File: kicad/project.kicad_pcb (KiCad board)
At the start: 2 copper layers, 22 parts, among them J1 SWD, SW1 SW_DPDT_x2, U1 STM32L031F4Px

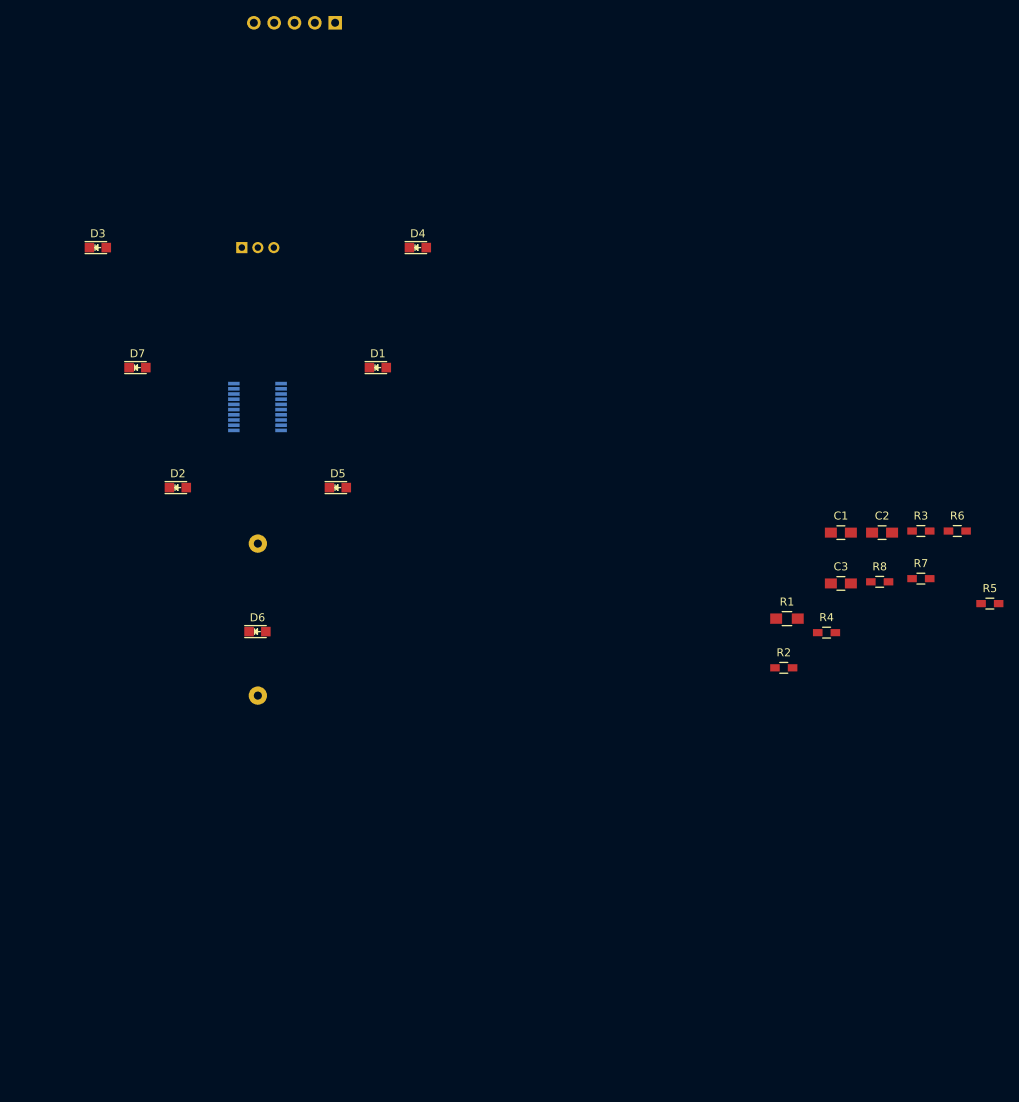
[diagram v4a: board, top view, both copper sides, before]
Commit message: Heart outline
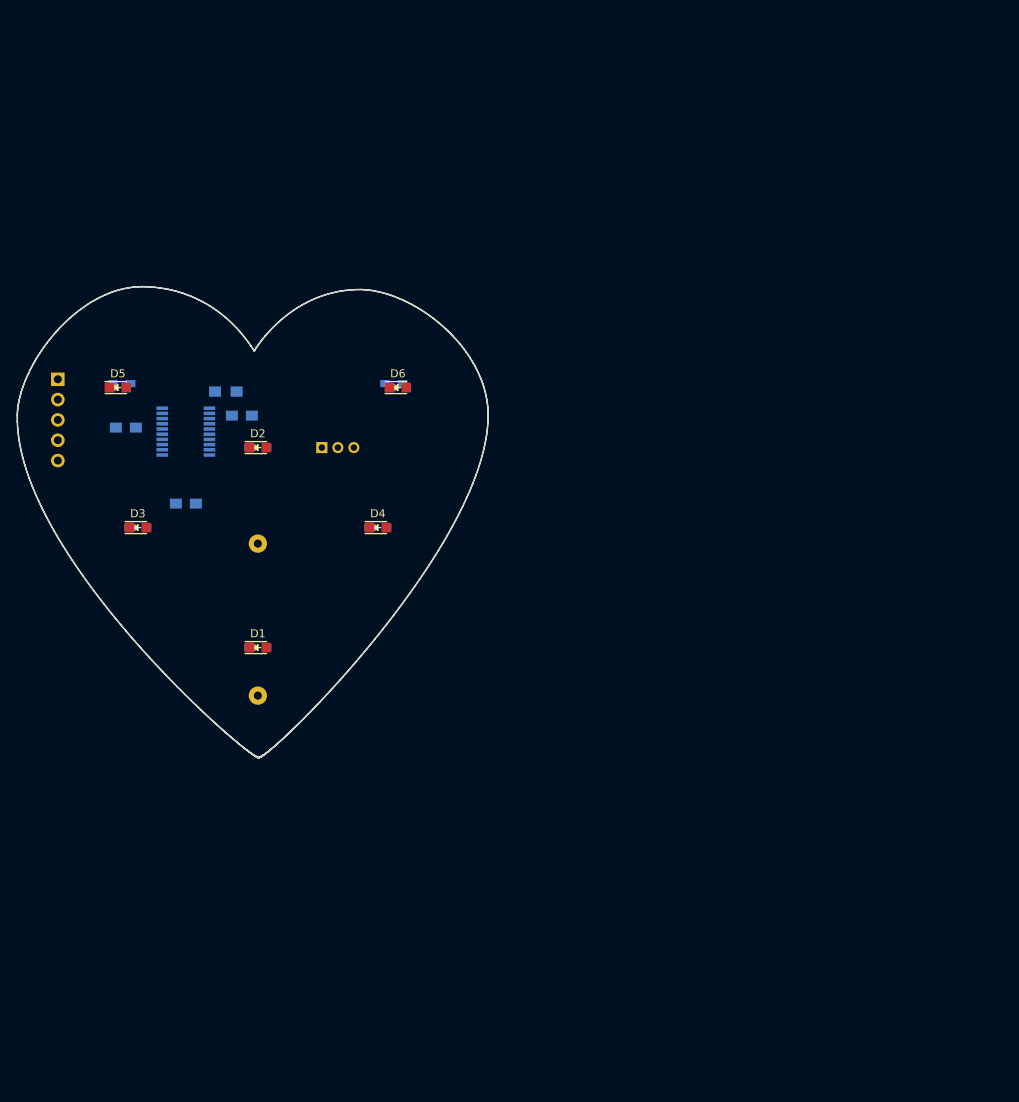
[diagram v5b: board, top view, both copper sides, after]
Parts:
- removed D7: LED, LEDs:LED_0805
- removed R8: 1k, Resistors_SMD:R_0603_HandSoldering
- C1, C2, C3, R1, R2, R3, R4, R5, R6, R7: moved to B.Cu
- moved R6 106.0 mm to (113.0, 97.0)
- moved C2 95.4 mm to (113.5, 102.5), turned to 180 degrees
- moved R4 87.1 mm to (115.0, 115.0), turned to 180 degrees
- moved R3 83.5 mm to (130.0, 105.0), turned to 180 degrees
- moved C1 82.0 mm to (121.0, 112.0), turned to 180 degrees
- moved C3 77.8 mm to (128.0, 101.0), turned to 180 degrees
- moved R5 77.1 mm to (145.0, 115.0), turned to 180 degrees
- moved R1 75.7 mm to (126.0, 98.0)
- moved R7 70.2 mm to (147.0, 97.0), turned to 180 degrees
- moved R2 65.8 mm to (130.0, 130.0), turned to 180 degrees
- moved J1 56.5 mm to (105.0, 96.5), turned to 180 degrees
- moved D1 38.1 mm to (130.0, 130.0)
- moved D3 35.4 mm to (115.0, 115.0)
- moved D4 35.4 mm to (145.0, 115.0)
- moved D6 35.2 mm to (147.5, 97.5)
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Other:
- board outline added: 58.9 x 58.9 mm

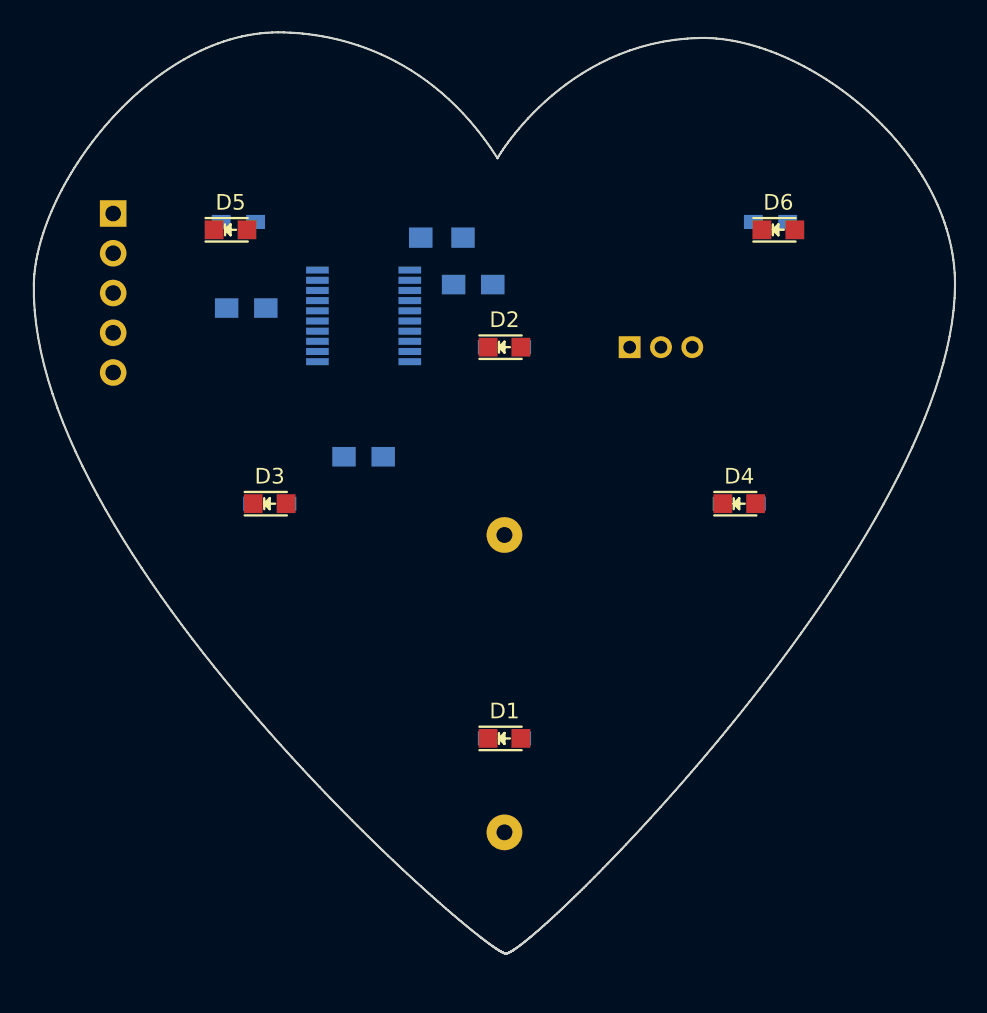
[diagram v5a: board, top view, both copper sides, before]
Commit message: Heart board outline
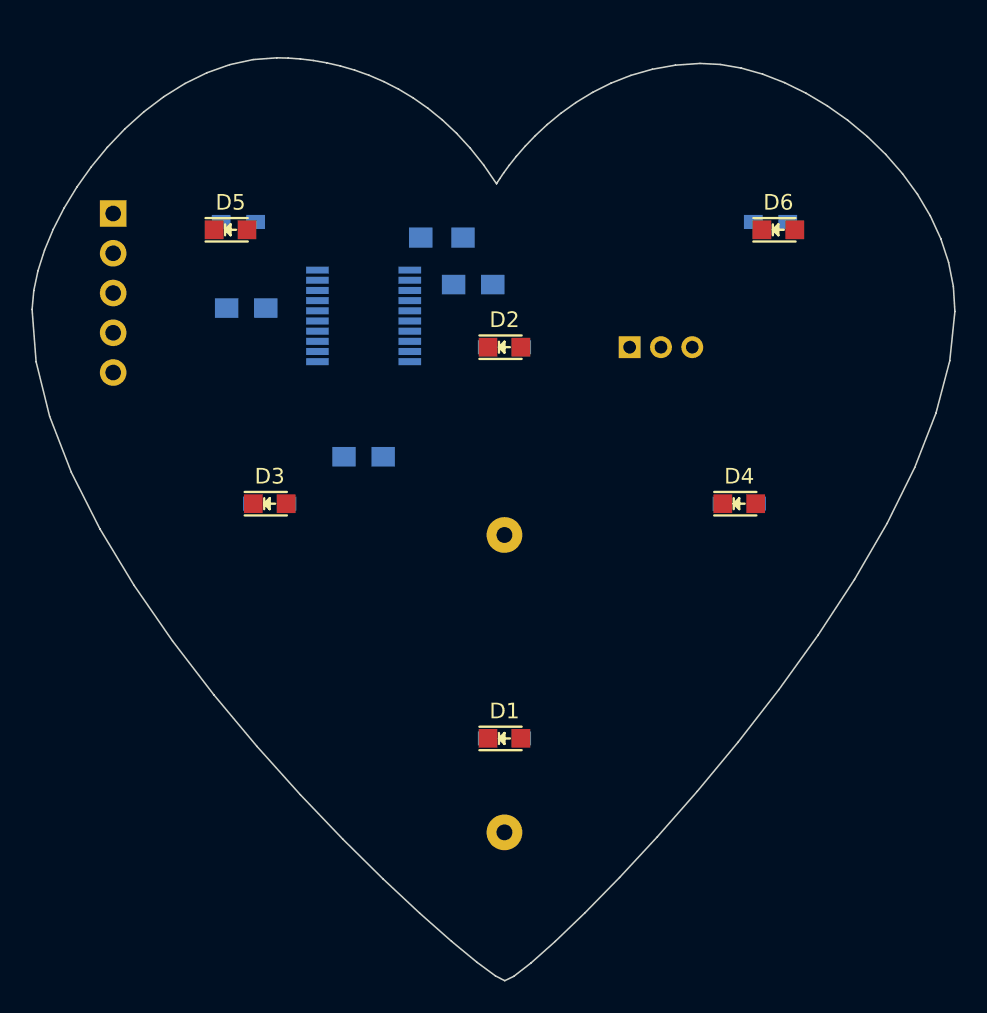
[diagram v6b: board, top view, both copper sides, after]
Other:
- board size 58.9 x 58.9 mm -> 59 x 59 mm
